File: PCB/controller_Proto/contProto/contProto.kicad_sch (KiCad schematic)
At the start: 21 parts, among them J1 Conn_01x05, J2 Conn_01x04, J3 Conn_01x05, J4 Conn_01x04, J5 Conn_01x05, J6 Conn_01x05, SW1 SMD_12x12mm_h8.5mm, SW2 SMD_12x12mm_h8.5mm, SW3 SMD_12x12mm_h8.5mm, SW4 SMD_12x12mm_h8.5mm, SW5 SMD_12x12mm_h8.5mm, SW6 SMD_12x12mm_h8.5mm, SW7 SMD_12x12mm_h8.5mm, U1 ProMicroC, U2 ProMicroC

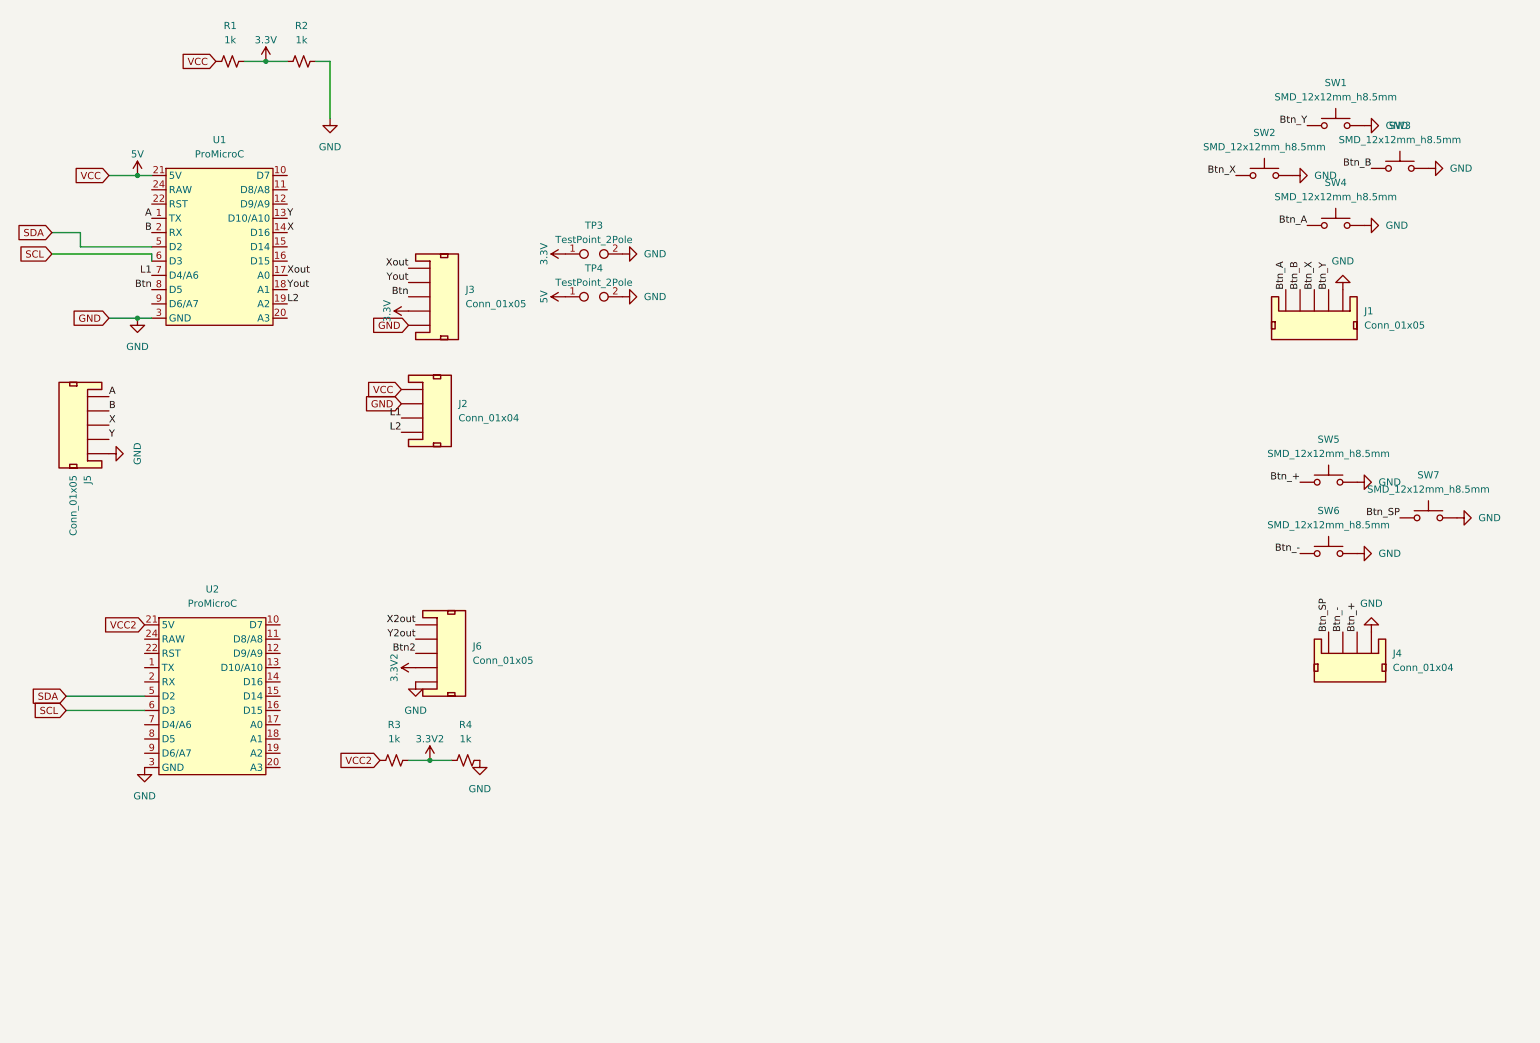
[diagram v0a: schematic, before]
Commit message: adding more buttons
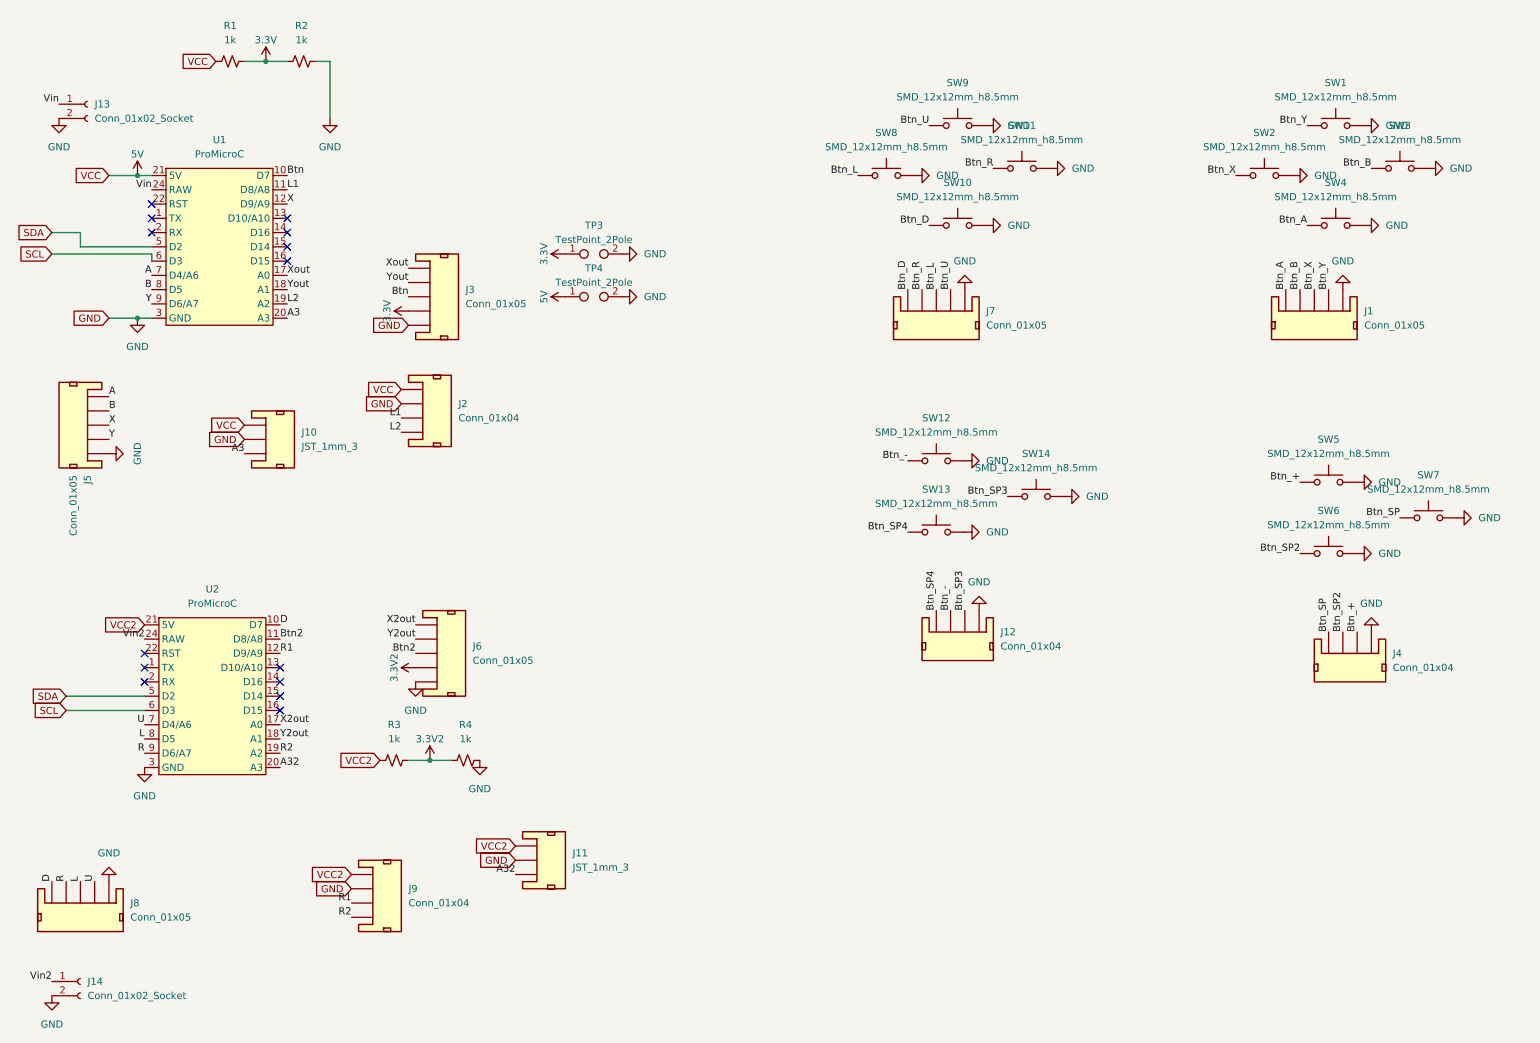
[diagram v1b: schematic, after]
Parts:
- added J10, J11: JST_1mm_3, PCM_SparkFun-Connector:JST_1x03_P1.0mm_Horizontal_SMD, symbol PCM_SparkFun-Connector:Conn_01x03_JST_P1.0mm_Horizontal_SMD
- added J12, J9: Conn_01x04, PCM_SparkFun-Connector:JST_1x04_P2.0mm_Horizontal_SMD, symbol PCM_SparkFun-Connector:Conn_01x04_JST_P2.0mm_Horizontal_SMD
- added J13, J14: Conn_01x02_Socket, symbol Connector:Conn_01x02_Socket
- added J7, J8: Conn_01x05, PCM_SparkFun-Connector:JST_1x05_P1.25mm_Locking_Horizontal_SMD, symbol PCM_SparkFun-Connector:Conn_01x05_JST_P1.0mm_Horizontal_SMD
- added SW10, SW11, SW12, SW13, SW14, SW8, SW9: SMD_12x12mm_h8.5mm, Button_Switch_SMD:SW_Push_1P1T_NO_CK_PTS125Sx73PSMTR, symbol PCM_SparkFun-Switch:SPST_Push_SMD_12x12mm_h8.5mm
- SW1, SW2, SW3, SW4, SW5, SW6, SW7: footprint PCM_SparkFun-Switch:Push_SMD_12x12mm -> Button_Switch_SMD:SW_Push_1P1T_NO_CK_PTS125Sx73PSMTR
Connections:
- net 5V: now also J10.1
- net A: now also U1.7 (D4/A6); no longer U1.1 (TX)
- net B: now also U1.8 (D5); no longer U1.2 (RX)
- net Btn: now also U1.10 (D7); no longer U1.8 (D5)
- net Btn2: now also U2.11 (D8/A8)
- net Btn_-: now also J12.3, SW12.1; no longer J4.3, SW6.1
- net GND: now also J10.2, J11.2, J12.1, J13.2 (Pin_2), J14.2 (Pin_2), J7.1, J8.1, J9.2, SW10.2, SW11.2, SW12.2, SW13.2, SW14.2, SW8.2, SW9.2
- net L1: now also U1.11 (D8/A8); no longer U1.7 (D4/A6)
- net VCC2: now also J11.1, J9.1
- net X: now also U1.12 (D9/A9); no longer U1.14 (D16)
- net X2out: now also U2.17 (A0)
- net Y: now also U1.9 (D6/A7); no longer U1.13 (D10/A10)
- net Y2out: now also U2.18 (A1)
- net D: now reaches U2.10 (D7)
- net D: now also J8.5
- net R1: now reaches U2.12 (D9/A9)
- net R1: now also J9.3
- net R2: now reaches U2.19 (A2)
- net R2: now also J9.4
- net A32: now reaches U2.20 (A3)
- net A32: now also J11.3
- net Vin2: now reaches U2.24 (RAW)
- net Vin2: now also J14.1 (Pin_1)
- net U: now reaches U2.7 (D4/A6)
- net U: now also J8.2
- net L: now reaches U2.8 (D5)
- net L: now also J8.3
- net R: now reaches U2.9 (D6/A7)
- net R: now also J8.4
- net A3: now reaches U1.20 (A3)
- net A3: now also J10.3
- net Vin: now reaches U1.24 (RAW)
- net Vin: now also J13.1 (Pin_1)
- new net Btn_D: J7.5, SW10.1
- new net Btn_L: J7.3, SW8.1
- new net Btn_R: J7.4, SW11.1
- new net Btn_SP2: J4.3, SW6.1
- new net Btn_SP3: J12.2, SW14.1
- new net Btn_SP4: J12.4, SW13.1
- new net Btn_U: J7.2, SW9.1
- no-connect marks 0 -> 14

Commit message: tinkering
need resistors on all buttons
ground needs to be separated still
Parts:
- added J15, J16: Conn_01x04, PCM_SparkFun-Connector:JST_1x04_P2.0mm_Horizontal_SMD, symbol PCM_SparkFun-Connector:Conn_01x04_JST_P2.0mm_Horizontal_SMD
- added SW15, SW16: SMD_12x12mm_h8.5mm, Button_Switch_SMD:SW_Tactile_SPST_NO_Straight_CK_PTS636Sx25SMTRLFS, symbol PCM_SparkFun-Switch:SPST_Push_SMD_12x12mm_h8.5mm
- added U3, U4: DRV5033FAxLPG, Package_TO_SOT_THT:TO-92_Inline, symbol Sensor_Magnetic:DRV5033FAxLPG
- SW1, SW10, SW11, SW12, SW13, SW14, SW2, SW3, SW4, SW5, SW6, SW7, SW8, SW9: footprint Button_Switch_SMD:SW_Push_1P1T_NO_CK_PTS125Sx73PSMTR -> Button_Switch_SMD:SW_Tactile_SPST_NO_Straight_CK_PTS636Sx25SMTRLFS
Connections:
- net L1: now also J9.3, U2.12 (D9/A9); no longer J2.3, U1.11 (D8/A8)
- net L2: now also J9.4, U2.19 (A2); no longer J2.4, U1.19 (A2)
- net R1: now also J2.3, U1.11 (D8/A8); no longer J9.3, U2.12 (D9/A9)
- net R2: now also J2.4, U1.19 (A2); no longer J9.4, U2.19 (A2)
- new net GND_LSP: J15.4, SW16.2, U3.2 (GND)
- new net GND_RSP: J16.4, SW15.2, U4.2 (GND)
- new net L1P: J15.1, SW16.1
- new net L2P: J15.2, U3.3 (OUT)
- new net R1P: J16.1, SW15.1
- new net R2P: J16.2, U4.3 (OUT)
- new net VCC_LSP: J15.3, U3.1 (VCC)
- new net VCC_RSP: J16.3, U4.1 (VCC)

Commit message: pcb fixing
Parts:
- removed J3, J6: Conn_01x05, PCM_SparkFun-Connector:JST_1x05_P1.25mm_Locking_Horizontal_SMD, symbol PCM_SparkFun-Connector:Conn_01x05_JST_P1.0mm_Horizontal_SMD
- removed TP3: TestPoint_2Pole, TestPoint:TestPoint_Bridge_Pitch2.0mm_Drill0.7mm, symbol Connector:TestPoint_2Pole
- added J17, J3: Conn_01x10_Pin, Connector_FFC-FPC:Amphenol_F32Q-1A7x1-11010_1x10-1MP_P0.5mm_Horizontal, symbol Connector:Conn_01x10_Pin
- added J18, J6: JST_1mm_3, PCM_SparkFun-Connector:JST_1x03_P1.0mm_Horizontal_SMD, symbol PCM_SparkFun-Connector:Conn_01x03_JST_P1.0mm_Horizontal_SMD
- added J19: Conn_01x08_Socket, Connector_PinSocket_1.00mm:PinSocket_1x08_P1.00mm_Vertical, symbol Connector:Conn_01x08_Socket
- added R10, R11, R12, R13, R14, R15, R16, R17, R18, R19, R20, R21, R22, R5, R6, R7, R8, R9: 1k, PCM_SparkFun-Resistor:R_0402_1005Metric, symbol PCM_SparkFun-Resistor:1k_0402
- added SW17, SW18: SMD_12x12mm_h8.5mm, Button_Switch_SMD:SW_Tactile_SPST_NO_Straight_CK_PTS636Sx25SMTRLFS, symbol PCM_SparkFun-Switch:SPST_Push_SMD_12x12mm_h8.5mm
- added TP1: TestPoint_2Pole, TestPoint:TestPoint_Bridge_Pitch2.0mm_Drill0.7mm, symbol Connector:TestPoint_2Pole
- J12, J15, J16, J2, J4, J9: footprint PCM_SparkFun-Connector:JST_1x04_P2.0mm_Horizontal_SMD -> PCM_SparkFun-Connector:JST_1x04_P1.25mm_Locking_Horizontal_SMD
- J13, J14: footprint (none) -> Connector_PinSocket_1.00mm:PinSocket_1x02_P1.00mm_Vertical
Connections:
- net 5V: now also J3.10 (Pin_10); no longer R1.1
- net Btn: now also J3.5 (Pin_5)
- net Btn2: now also J17.5 (Pin_5)
- net GND: now also R1.2, R3.2, J17.2 (Pin_2), J17.4 (Pin_4), J17.8 (Pin_8), J18.3, J3.2 (Pin_2), J3.4 (Pin_4), J3.8 (Pin_8), J6.3, R10.2, R11.2, R12.2, R13.2, R14.2, R15.2, R16.2, R17.2, R18.2, R19.2, R20.2, R21.2, R22.2, R5.2, R6.2, R7.2, R8.2, R9.2, TP1.2; no longer J1.1, J12.1, J4.1, J7.1, SW1.2, SW10.2, SW11.2, SW12.2, SW13.2, SW14.2, SW2.2, SW3.2, SW4.2, SW5.2, SW6.2, SW7.2, SW8.2, SW9.2
- net GND_LSP: no longer SW16.2
- net GND_RSP: no longer SW15.2
- net VCC2: now also J17.10 (Pin_10), TP1.1; no longer R3.1
- net VCC_LSP: now also SW16.2
- net VCC_RSP: now also SW15.2
- net X2out: now also J17.6 (Pin_6)
- net Xout: now also J3.6 (Pin_6)
- net Y2out: now also J17.9 (Pin_9)
- net Yout: now also J3.9 (Pin_9)
- net Pad3: now reaches U2.15 (D14)
- net Pad3: now also J6.2
- net Pad4: now reaches U2.16 (D15)
- net Pad4: now also J6.1
- net RST2: now reaches U2.22 (RST)
- net Pad1: now reaches U1.15 (D14)
- net Pad1: now also J18.2
- net Pad2: now reaches U1.16 (D15)
- net Pad2: now also J18.1
- net 3.3V: no longer names the net of R2.1
- net 3.3V: no longer R1.2
- net 3.3V2: no longer names the net of R4.1
- net 3.3V2: no longer R3.2
- no-connect marks 14 -> 18

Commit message: fixing pcb
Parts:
- removed J12, J4: Conn_01x04, PCM_SparkFun-Connector:JST_1x04_P1.25mm_Locking_Horizontal_SMD, symbol PCM_SparkFun-Connector:Conn_01x04_JST_P2.0mm_Horizontal_SMD
- removed SW13, SW6: SMD_12x12mm_h8.5mm, Button_Switch_SMD:SW_Tactile_SPST_NO_Straight_CK_PTS636Sx25SMTRLFS, symbol PCM_SparkFun-Switch:SPST_Push_SMD_12x12mm_h8.5mm
- added J12, J20, J21, J4: JST_1mm_3, Connector_JST:JST_GH_BM03B-GHS-TBT_1x03-1MP_P1.25mm_Vertical, symbol PCM_SparkFun-Connector:Conn_01x03_JST_P1.0mm_Horizontal_SMD
- J1, J5, J7, J8: footprint PCM_SparkFun-Connector:JST_1x05_P1.25mm_Locking_Horizontal_SMD -> Connector_JST:JST_GH_BM05B-GHS-TBT_1x05-1MP_P1.25mm_Vertical
- J10, J11, J18, J6: footprint PCM_SparkFun-Connector:JST_1x03_P1.0mm_Horizontal_SMD -> Connector_JST:JST_GH_BM03B-GHS-TBT_1x03-1MP_P1.25mm_Vertical
- J15, J16, J2, J9: footprint PCM_SparkFun-Connector:JST_1x04_P1.25mm_Locking_Horizontal_SMD -> Connector_JST:JST_GH_BM04B-GHS-TBT_1x04-1MP_P1.25mm_Vertical
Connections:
- net 5V: now also J18.3, J5.1, SW18.2, J21.1
- net A: now also R4.1
- net B: now also R14.1
- net Btn_+: now also J4.2
- net Btn_-: now also J12.3
- net Btn_SP2: now also J4.3
- net Btn_SP3: now also J12.2
- net D: now also R21.1
- net GND: now also J19.2 (Pin_2); no longer J18.3, J5.1, J6.3, J8.1
- net L: now also R7.1
- net L1: now also R3.1
- net Pad1: now also R15.1
- net Pad2: now also R10.1
- net Pad3: now also R17.1
- net Pad4: now also R11.1
- net R: now also R16.1
- net R1: now also R9.1
- net RST2: now also R13.1, SW17.1
- net SCL: now also J19.3 (Pin_3)
- net SDA: now also J19.4 (Pin_4)
- net U: now also R6.1
- net VCC2: now also J19.1 (Pin_1), J6.3, J8.1, SW17.2, J20.1
- net X: now also R1.1
- net Y: now also R2.1
- net RST1: now reaches SW18.1
- net RST1: now also R19.1, U1.22 (RST)
- net FB_VCC: now reaches SW4.2
- net FB_VCC: now also J1.1, SW1.2, SW2.2, SW3.2
- net minus: now reaches U2.13 (D10/A10)
- net minus: now also R8.1, J20.3
- net SP3: now reaches U2.14 (D16)
- net SP3: now also R5.1, J20.2
- net SL_VCC: now reaches SW14.2
- net SL_VCC: now also SW12.2, J12.1
- net SR_VCC: now reaches SW7.2
- net SR_VCC: now also SW5.2, J4.1
- net AD0: now reaches J19.7 (Pin_7)
- net D_VCC: now reaches SW10.2
- net D_VCC: now also J7.1, SW11.2, SW8.2, SW9.2
- net SP2: now reaches U1.13 (D10/A10)
- net SP2: now also R20.1, J21.3
- net plus: now reaches U1.14 (D16)
- net plus: now also R22.1, J21.2
- no-connect marks 18 -> 15
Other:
- moved on the sheet: J19, R1, R11, R12, R13, R14, R16, R18, R19, R2, R20, R21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

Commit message: PCB layout
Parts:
- added J22, J23: JST_1mm_3, Connector_JST:JST_GH_BM03B-GHS-TBT_1x03-1MP_P1.25mm_Vertical, symbol PCM_SparkFun-Connector:Conn_01x03_JST_P1.0mm_Horizontal_SMD
- added SW13, SW19, SW20, SW6: SMD_12x12mm_h8.5mm, Button_Switch_SMD:SW_Tactile_SPST_NO_Straight_CK_PTS636Sx25SMTRLFS, symbol PCM_SparkFun-Switch:SPST_Push_SMD_12x12mm_h8.5mm
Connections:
- net Btn_SP is gone; now on net Btn_SP2: SW7.1
- net Btn: now also R12.1
- net Btn2: now also R18.1
- new net PP1: J23.2, SW13.1
- new net PP2: J23.3, SW6.1
- new net PP3: J22.2, SW19.1
- new net PP4: J22.3, SW20.1
- new net PPVCC1: J23.1, SW13.2, SW6.2
- new net PPVCC2: J22.1, SW19.2, SW20.2
- no-connect marks 15 -> 14
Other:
- moved on the sheet: J12, J4

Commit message: finnish shoulder borads
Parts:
- added J24, J25, J26, J27: Conn_01x03_Socket, Connector_PinSocket_2.54mm:PinSocket_1x03_P2.54mm_Vertical, symbol Connector:Conn_01x03_Socket
- added J28, J29, J30, J31: Conn_01x12_Socket, Connector_PinSocket_2.54mm:PinSocket_1x12_P2.54mm_Vertical, symbol Connector:Conn_01x12_Socket
- J19: footprint Connector_PinSocket_1.00mm:PinSocket_1x08_P1.00mm_Vertical -> Connector_PinSocket_2.54mm:PinSocket_1x08_P2.54mm_Vertical
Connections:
- net 5V: now also J29.9 (Pin_9)
- net A: now also J28.7 (Pin_7)
- net A3: now also J29.8 (Pin_8)
- net A32: now also J31.5 (Pin_5)
- net B: now also J28.8 (Pin_8)
- net Btn: now also J28.10 (Pin_10)
- net Btn2: now also J30.11 (Pin_11)
- net D: now also J30.10 (Pin_10)
- net GND: now also J28.3 (Pin_3), J28.4 (Pin_4), J29.11 (Pin_11), J30.3 (Pin_3), J30.4 (Pin_4), J31.2 (Pin_2)
- net GND_LSP: now also J27.1 (Pin_1); no longer U3.2 (GND)
- net GND_RSP: now also J24.1 (Pin_1); no longer U4.2 (GND)
- net L: now also J30.8 (Pin_8)
- net L1: now also J30.12 (Pin_12)
- net L2: now also J31.6 (Pin_6)
- net L2P: now also J27.3 (Pin_3); no longer U3.3 (OUT)
- net Pad1: now also J29.3 (Pin_3)
- net Pad2: now also J29.4 (Pin_4)
- net Pad3: now also J31.10 (Pin_10)
- net Pad4: now also J31.9 (Pin_9)
- net R: now also J30.9 (Pin_9)
- net R1: now also J28.11 (Pin_11)
- net R2: now also J29.7 (Pin_7)
- net R2P: now also J24.3 (Pin_3); no longer U4.3 (OUT)
- net RST1: now also J29.10 (Pin_10)
- net RST2: now also J31.3 (Pin_3)
- net SCL: now also J28.6 (Pin_6), J30.6 (Pin_6)
- net SDA: now also J28.5 (Pin_5), J30.5 (Pin_5)
- net SP2: now also J29.1 (Pin_1)
- net SP3: now also J31.11 (Pin_11)
- net U: now also J30.7 (Pin_7)
- net VCC2: now also J31.4 (Pin_4)
- net VCC_LSP: now also J27.2 (Pin_2); no longer U3.1 (VCC)
- net VCC_RSP: now also J24.2 (Pin_2); no longer U4.1 (VCC)
- net Vin: now also J29.12 (Pin_12)
- net Vin2: now also J31.1 (Pin_1)
- net X: now also J28.12 (Pin_12)
- net X2out: now also J31.8 (Pin_8)
- net Xout: now also J29.5 (Pin_5)
- net Y: now also J28.9 (Pin_9)
- net Y2out: now also J31.7 (Pin_7)
- net Yout: now also J29.6 (Pin_6)
- net minus: now also J31.12 (Pin_12)
- net plus: now also J29.2 (Pin_2)
- new net GND_LSP2: J26.2 (Pin_2), U3.2 (GND)
- new net GND_RSP2: J25.2 (Pin_2), U4.2 (GND)
- new net L2P2: J26.3 (Pin_3), U3.3 (OUT)
- new net R2P2: J25.3 (Pin_3), U4.3 (OUT)
- new net VCC_LSP2: J26.1 (Pin_1), U3.1 (VCC)
- new net VCC_RSP2: J25.1 (Pin_1), U4.1 (VCC)
- no-connect marks 14 -> 18
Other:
- moved on the sheet: SW17, SW18

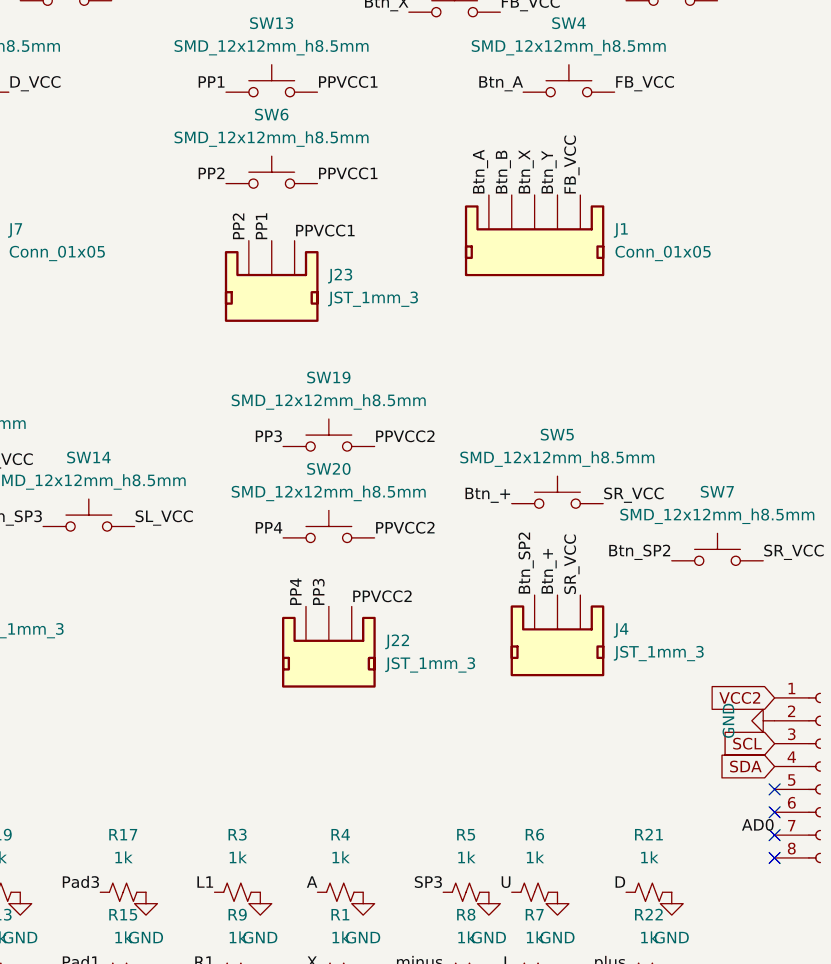
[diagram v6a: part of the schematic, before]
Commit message: failing with mouse bites
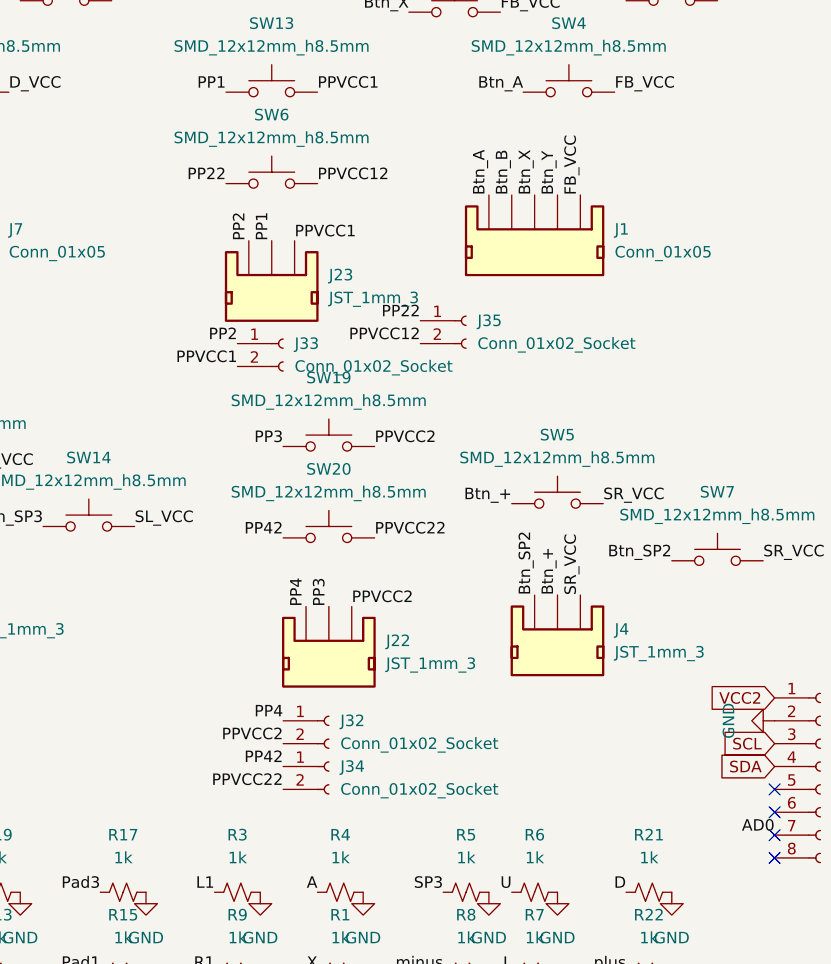
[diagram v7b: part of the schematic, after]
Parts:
- added J32, J33, J34, J35: Conn_01x02_Socket, Connector_PinSocket_2.54mm:PinSocket_1x02_P2.54mm_Vertical, symbol Connector:Conn_01x02_Socket
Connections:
- net PP2: now also J33.1 (Pin_1); no longer SW6.1
- net PP4: now also J32.1 (Pin_1); no longer SW20.1
- net PPVCC1: now also J33.2 (Pin_2); no longer SW6.2
- net PPVCC2: now also J32.2 (Pin_2); no longer SW20.2
- new net PP22: J35.1 (Pin_1), SW6.1
- new net PP42: J34.1 (Pin_1), SW20.1
- new net PPVCC12: J35.2 (Pin_2), SW6.2
- new net PPVCC22: J34.2 (Pin_2), SW20.2
